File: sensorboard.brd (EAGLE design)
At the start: 87.3 x 55.9 mm, 43 parts, among them U1 LM1117MP-3.3, U2 LM324D

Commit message: preliminary placement
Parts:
- moved U$1 53.6 mm to (27.9, 59.7), turned to 270 degrees
- moved X3 49.0 mm to (47.0, 14.0), turned to 90 degrees
- moved R7 45.4 mm to (20.3, 66.0)
- moved R8 45.4 mm to (20.3, 68.6)
- moved D4 44.0 mm to (38.1, 49.5)
- moved U$3 41.8 mm to (62.2, 3.81)
- moved D3 40.5 mm to (49.5, 67.3)
- moved JP5 38.7 mm to (49.5, 27.9), turned to 90 degrees
- moved R11 36.1 mm to (14.0, 17.8), turned to 90 degrees
- moved U1 35.8 mm to (31.8, 67.3)
- moved R6 34.9 mm to (20.3, 63.5)
- moved R13 34.3 mm to (39.4, 68.6)
- moved JP1 34.2 mm to (53.3, 35.6), turned to 90 degrees
- moved R5 33.9 mm to (19.1, 57.1)
- moved R17 33.5 mm to (40.6, 62.2)
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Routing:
- net N$8: track 0.00 -> 32.8 mm
- net N$9: track 0.00 -> 29.4 mm
- net N$10: track 0.00 -> 25.9 mm
- net N$23: track 0.00 -> 24.1 mm
- net N$22: track 0.00 -> 21.5 mm
- net N$11: track 0.00 -> 20.7 mm, vias 0 -> 1
- net N$12: track 0.00 -> 18.4 mm
- net N$21: track 0.00 -> 18.1 mm
- net N$20: track 0.00 -> 16.7 mm
- net N$19: track 0.00 -> 15.9 mm
- net N$13: track 0.00 -> 15.8 mm
- net N$18: track 0.00 -> 15.2 mm
- net N$14: track 0.00 -> 13.6 mm
- net N$17: track 0.00 -> 13.6 mm
- net N$15: track 0.00 -> 11.8 mm
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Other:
- board size 87.3 x 55.9 mm -> 56 x 78 mm

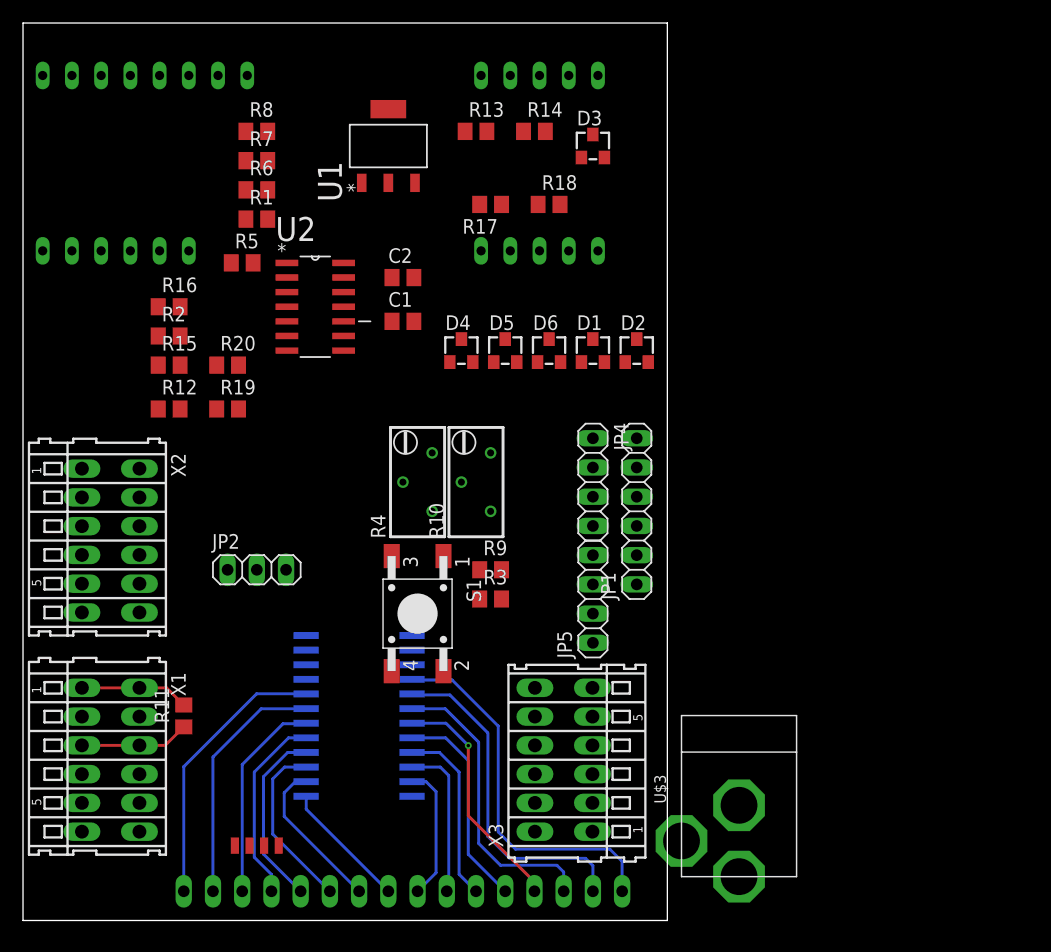
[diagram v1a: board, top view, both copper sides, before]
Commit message: changed HYT271 from SMD to THT
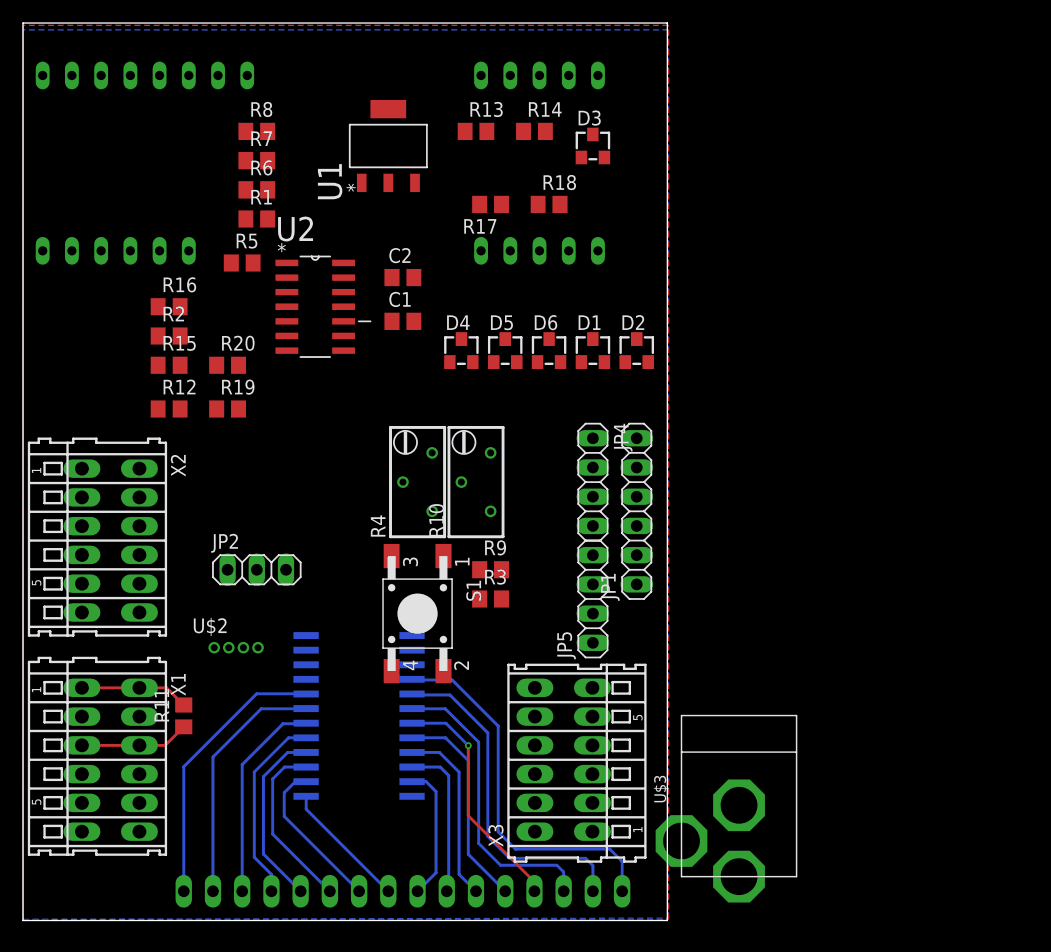
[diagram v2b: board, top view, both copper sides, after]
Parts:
- U$2: value HYT271 -> HYT271-THT; device humidity:HYT271 -> humidity:HYT271-THT
- moved U$2 7.42 mm to (18.5, 23.7)
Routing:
- added copper zone on layer 1, net GND
- added copper zone on layer 16, net GND
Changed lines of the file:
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@@
 <attribute name="OC_FARNELL" value="1283536" x="-55.88" y="-7.62" size="1.778" layer="27" rot="R270" display="off"/>
 </element>
-<element name="U$2" library="humidity" package="HYT271" value="HYT271" x="20.32" y="16.51"/>
+<element name="U$2" library="humidity" package="HYT271-THT" value="HYT271-THT" x="18.52" y="23.71"/>
 <element name="X2" library="con-wago" package="233-206" value="" x="7.62" y="33.02" rot="R270">
 <attribute name="OC_NEWARK" value="28K9063" x="-55.88" y="-6.35" size="1.778" layer="27" rot="R270" display="off"/>
@@
 <contactref element="U$4" pad="P$3"/>
 <contactref element="U$4" pad="P$2"/>
-<wire x1="48.53" y1="48.53" x2="48.53" y2="66.31" width="0" layer="19" extent="1-1"/>
-<wire x1="52.34" y1="48.53" x2="48.53" y2="48.53" width="0" layer="19" extent="1-1"/>
-<wire x1="44.72" y1="48.53" x2="48.53" y2="48.53" width="0" layer="19" extent="1-1"/>
-<wire x1="40.91" y1="48.53" x2="44.72" y2="48.53" width="0" layer="19" extent="1-1"/>
-<wire x1="37.1" y1="48.53" x2="40.91" y2="48.53" width="0" layer="19" extent="1-1"/>
-<wire x1="33.97" y1="52.07" x2="37.1" y2="48.53" width="0" layer="19" extent="1-1"/>
-<wire x1="33.97" y1="55.88" x2="33.97" y2="52.07" width="0" layer="19" extent="1-1"/>
-<wire x1="27.8638" y1="53.34" x2="33.97" y2="52.07" width="0" layer="19" extent="1-1"/>
-<wire x1="53.34" y1="39.37" x2="52.34" y2="48.53" width="0" layer="19" extent="1-1"/>
-<wire x1="29.4386" y1="64.1096" x2="33.97" y2="55.88" width="0" layer="19" extent="1-1"/>
-<wire x1="18.1" y1="57.15" x2="27.8638" y2="53.34" width="0" layer="19" extent="1-1"/>
-<wire x1="40.64" y1="35.56" x2="40.91" y2="48.53" width="0" layer="19" extent="1-1"/>
-<wire x1="35.56" y1="35.56" x2="40.64" y2="35.56" width="0" layer="19" extent="1-1"/>
-<wire x1="32.04" y1="31.67" x2="35.56" y2="35.56" width="0" layer="19" extent="1-1"/>
-<wire x1="33.81" y1="24.765" x2="32.04" y2="31.67" width="0" layer="19" extent="1-16"/>
-<wire x1="33.81" y1="23.495" x2="33.81" y2="24.765" width="0" layer="19" extent="16-16"/>
-<wire x1="33.81" y1="22.225" x2="33.81" y2="23.495" width="0" layer="19" extent="16-16"/>
-<wire x1="32.04" y1="21.67" x2="33.81" y2="22.225" width="0" layer="19" extent="1-16"/>
-<wire x1="33.81" y1="10.795" x2="32.04" y2="21.67" width="0" layer="19" extent="1-16"/>
-<wire x1="17.78" y1="30.48" x2="32.04" y2="31.67" width="0" layer="19" extent="1-1"/>
-<wire x1="19.685" y1="6.51" x2="33.81" y2="10.795" width="0" layer="19" extent="1-16"/>
-<wire x1="5.12" y1="7.72" x2="19.685" y2="6.51" width="0" layer="19" extent="1-1"/>
-<wire x1="5.12" y1="12.72" x2="5.12" y2="7.72" width="0" layer="19" extent="1-1"/>
-<wire x1="5.12" y1="17.72" x2="5.12" y2="12.72" width="0" layer="19" extent="1-1"/>
-<wire x1="1.71" y1="73.44" x2="18.1" y2="57.15" width="0" layer="19" extent="1-1"/>
-<wire x1="62.23" y1="10.01" x2="33.81" y2="10.795" width="0" layer="19" extent="16-16"/>
+<polygon width="0.4064" layer="1">
+<vertex x="56.1" y="0.1"/>
+<vertex x="56.1" y="77.8"/>
+<vertex x="0" y="77.8"/>
+<vertex x="0" y="0"/>
+</polygon>
+<polygon width="0.4064" layer="16">
+<vertex x="56.1" y="0.2"/>
+<vertex x="56.1" y="77.4"/>
+<vertex x="0" y="77.4"/>
+<vertex x="0" y="0.1"/>
+</polygon>
+<wire x1="33.81" y1="10.795" x2="62.23" y2="10.01" width="0" layer="19" extent="16-16"/>
+<wire x1="17.885" y1="23.71" x2="17.78" y2="30.48" width="0" layer="19" extent="1-1"/>
 </signal>
 <signal name="+3V3">
@@
 <wire x1="22.86" y1="30.48" x2="18.73" y2="44.45" width="0" layer="19" extent="1-1"/>
 <wire x1="24.61" y1="24.765" x2="22.86" y2="30.48" width="0" layer="19" extent="16-16"/>
-<wire x1="13.97" y1="18.73" x2="24.61" y2="24.765" width="0" layer="19" extent="1-16"/>
-<wire x1="20.955" y1="6.51" x2="13.97" y2="18.73" width="0" layer="19" extent="1-1"/>
+<wire x1="19.155" y1="23.71" x2="24.61" y2="24.765" width="0" layer="19" extent="16-16"/>
+<wire x1="13.97" y1="18.73" x2="19.155" y2="23.71" width="0" layer="19" extent="1-1"/>
 <wire x1="41.59" y1="27.94" x2="24.61" y2="24.765" width="0" layer="19" extent="1-16"/>
 <wire x1="53.34" y1="41.91" x2="41.59" y2="27.94" width="0" layer="19" extent="1-1"/>
@@
 <contactref element="R2" pad="1"/>
 <wire x1="24.61" y1="23.495" x2="53.34" y2="29.21" width="0" layer="19" extent="16-16"/>
-<wire x1="18.415" y1="6.51" x2="24.61" y2="23.495" width="0" layer="19" extent="1-16"/>
-<wire x1="5.12" y1="31.77" x2="24.61" y2="23.495" width="0" layer="19" extent="16-16"/>
+<wire x1="16.615" y1="23.71" x2="24.61" y2="23.495" width="0" layer="19" extent="16-16"/>
+<wire x1="5.12" y1="31.77" x2="16.615" y2="23.71" width="0" layer="19" extent="1-1"/>
 <wire x1="11.75" y1="50.8" x2="5.12" y2="31.77" width="0" layer="19" extent="1-1"/>
 <wire x1="9.33" y1="58.2" x2="11.75" y2="50.8" width="0" layer="19" extent="1-1"/>
@@
 <contactref element="R19" pad="1"/>
 <wire x1="24.61" y1="22.225" x2="53.34" y2="31.75" width="0" layer="19" extent="16-16"/>
-<wire x1="22.225" y1="6.51" x2="24.61" y2="22.225" width="0" layer="19" extent="1-16"/>
-<wire x1="5.12" y1="29.27" x2="24.61" y2="22.225" width="0" layer="19" extent="16-16"/>
+<wire x1="20.425" y1="23.71" x2="24.61" y2="22.225" width="0" layer="19" extent="16-16"/>
+<wire x1="5.12" y1="29.27" x2="20.425" y2="23.71" width="0" layer="19" extent="1-1"/>
 <wire x1="16.83" y1="44.45" x2="5.12" y2="29.27" width="0" layer="19" extent="1-1"/>
 <wire x1="11.87" y1="58.2" x2="16.83" y2="44.45" width="0" layer="19" extent="1-1"/>

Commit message: routing
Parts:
- removed JP1: (no value), pinhead:1X06
- removed JP2: (no value), pinhead:1X03
- removed JP3: (no value), pinhead:1X16
- removed JP4: (no value), pinhead:1X04
- removed R19, R2, R20: 10k, rcl:R0805
- removed U$4: PCA9532D, philips:SO24
- added JP6: (no value), pinhead:1X04
- added U$5: DS18S20, dallas:TO-92
- U$3: value HOHLBUCHSE -> BMP085; device Ergaenzung:HOHLBUCHSE -> humidity:BREAKOUT
- moved R16 45.0 mm to (48.0, 25.5), turned to 270 degrees
- moved R14 43.1 mm to (42.9, 25.5), turned to 270 degrees
- moved R13 43.1 mm to (40.4, 25.5), turned to 270 degrees
- moved JP5 42.9 mm to (6.61, 27.8)
- moved U$3 41.7 mm to (22.8, 17.4), turned to 0 degrees
- moved R15 39.9 mm to (45.5, 25.5), turned to 270 degrees
- moved R17 38.0 mm to (50.6, 25.5), turned to 270 degrees
- moved R18 37.5 mm to (53.1, 25.5), turned to 270 degrees
- moved R12 35.0 mm to (36.8, 19.1), turned to 90 degrees
- moved X2 30.6 mm to (29.0, 11.1)
- moved R11 25.2 mm to (11.2, 42.9), turned to 180 degrees
- moved R8 25.0 mm to (33.0, 47.0)
- moved S1 22.7 mm to (11.6, 27.4)
- moved R7 20.8 mm to (33.0, 49.5), turned to 180 degrees
- moved R10 19.4 mm to (20.3, 34.3), turned to 90 degrees
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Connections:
- removed net !RESET: R20.1, U$4.P$21
- removed net EOC: JP1.4
- removed net N$10: JP3.3, U$4.P$6
- removed net N$11: JP3.4, U$4.P$7
- removed net N$12: JP3.5, U$4.P$8
- removed net N$13: JP3.6, U$4.P$9
- removed net N$14: JP3.7, U$4.P$10
- removed net N$15: JP3.8, U$4.P$11
- removed net N$16: JP3.9, U$4.P$13
- removed net N$17: JP3.10, U$4.P$14
- removed net N$18: JP3.11, U$4.P$15
- removed net N$19: JP3.12, U$4.P$16
- removed net N$20: JP3.13, U$4.P$17
- removed net N$21: JP3.14, U$4.P$18
- removed net N$22: JP3.15, U$4.P$19
- removed net N$23: JP3.16, U$4.P$20
- removed net N$8: JP3.1, U$4.P$4
- removed net N$9: JP3.2, U$4.P$5
- removed net PF3: U$1.PD3
- removed net XCLR: JP1.3
- net +3V3: now also U$3.VCC, U$5.VDD; no longer JP1.6, JP2.3, R19.2, R2.2, R20.2, U$4.P$24
- net +5V: no longer U$3.I
- net DQ: now also U$5.DQ; no longer JP2.2
- net GND: now also U$3.GND, U$5.GND; no longer JP1.5, JP2.1, U$3.O, U$4.P$1, U$4.P$12, U$4.P$2, U$4.P$3
- net PB0: now also JP6.1; no longer JP4.1
- net PB1: now also JP6.2; no longer JP4.2
- net PB2: now also JP6.3; no longer JP4.3
- net PB3: now also JP6.4; no longer JP4.4
- net PD3: now also U$1.PD3
- net SCL: now also U$3.SCL; no longer JP1.2, R19.1, U$4.P$22
- net SDA: now also U$3.SDA; no longer JP1.1, R2.1, U$4.P$23
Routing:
- net +3V3: track 9.47 -> 145.8 mm, vias 0 -> 5
- net S1: track 0.00 -> 118.6 mm
- net PC7: track 0.00 -> 98.1 mm
- net DQ: track 0.00 -> 75.4 mm
- net MOSI: track 0.00 -> 74.0 mm, vias 0 -> 1
- net +5V: track 9.52 -> 76.2 mm, vias 0 -> 4
- net SCLK: track 0.00 -> 63.4 mm
- net MISO: track 0.00 -> 59.2 mm, vias 0 -> 1
- net PT100: track 0.00 -> 58.6 mm, vias 0 -> 3
- net SDA: track 0.00 -> 56.0 mm
- net SCL: track 0.00 -> 54.5 mm
- net TEMPERATURE: track 0.00 -> 48.7 mm, vias 0 -> 2
- net IO3: track 0.00 -> 45.9 mm, vias 0 -> 1
- net IO2: track 0.00 -> 45.4 mm, vias 0 -> 1
- net IO1: track 0.00 -> 45.2 mm, vias 0 -> 1
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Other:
- board size 56 x 78 mm -> 56 x 71 mm

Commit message: organized placement print
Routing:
- net +3V3: track 145.8 -> 147.5 mm
- net DQ: track 75.4 -> 74.4 mm
- net PT100: track 58.6 -> 57.7 mm
- net GND: vias 7 -> 8

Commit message: added version number
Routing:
- net PT100: track 57.7 -> 58.7 mm
- net PB3: track 44.5 -> 45.3 mm
- net S1: track 118.6 -> 119.4 mm
- net N$5: track 27.6 -> 28.3 mm
- net GND: vias 8 -> 9
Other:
- board text added: "20130904"
- board text added: "hexabus sensorboard"
